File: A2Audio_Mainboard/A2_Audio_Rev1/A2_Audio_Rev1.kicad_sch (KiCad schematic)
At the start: 33 parts, among them J2 AudioJack3, J3 BOOT_JUMPER, SW1 SW_Push, SW2 WIFI_SLIDER, SW3 RotaryEncoder_Switch, SW4 BT_SLIDER, SW5 SW_PREV, SW6 SW_NEXT, SW7 SW_PLAY, U15 CM5108000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

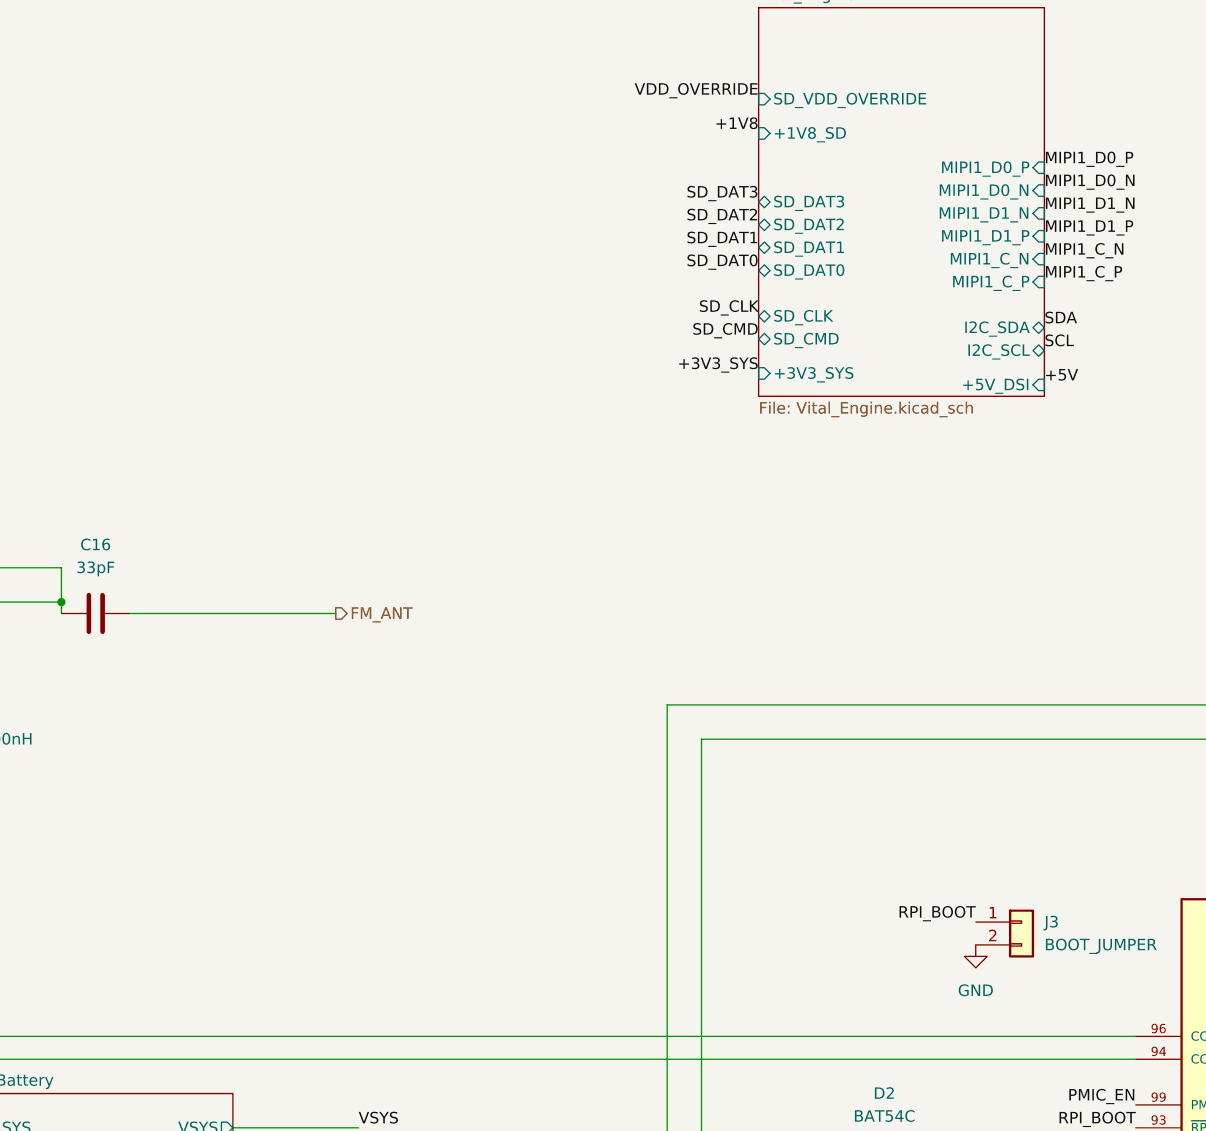
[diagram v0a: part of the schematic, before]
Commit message: Added footprints and a few more parts.
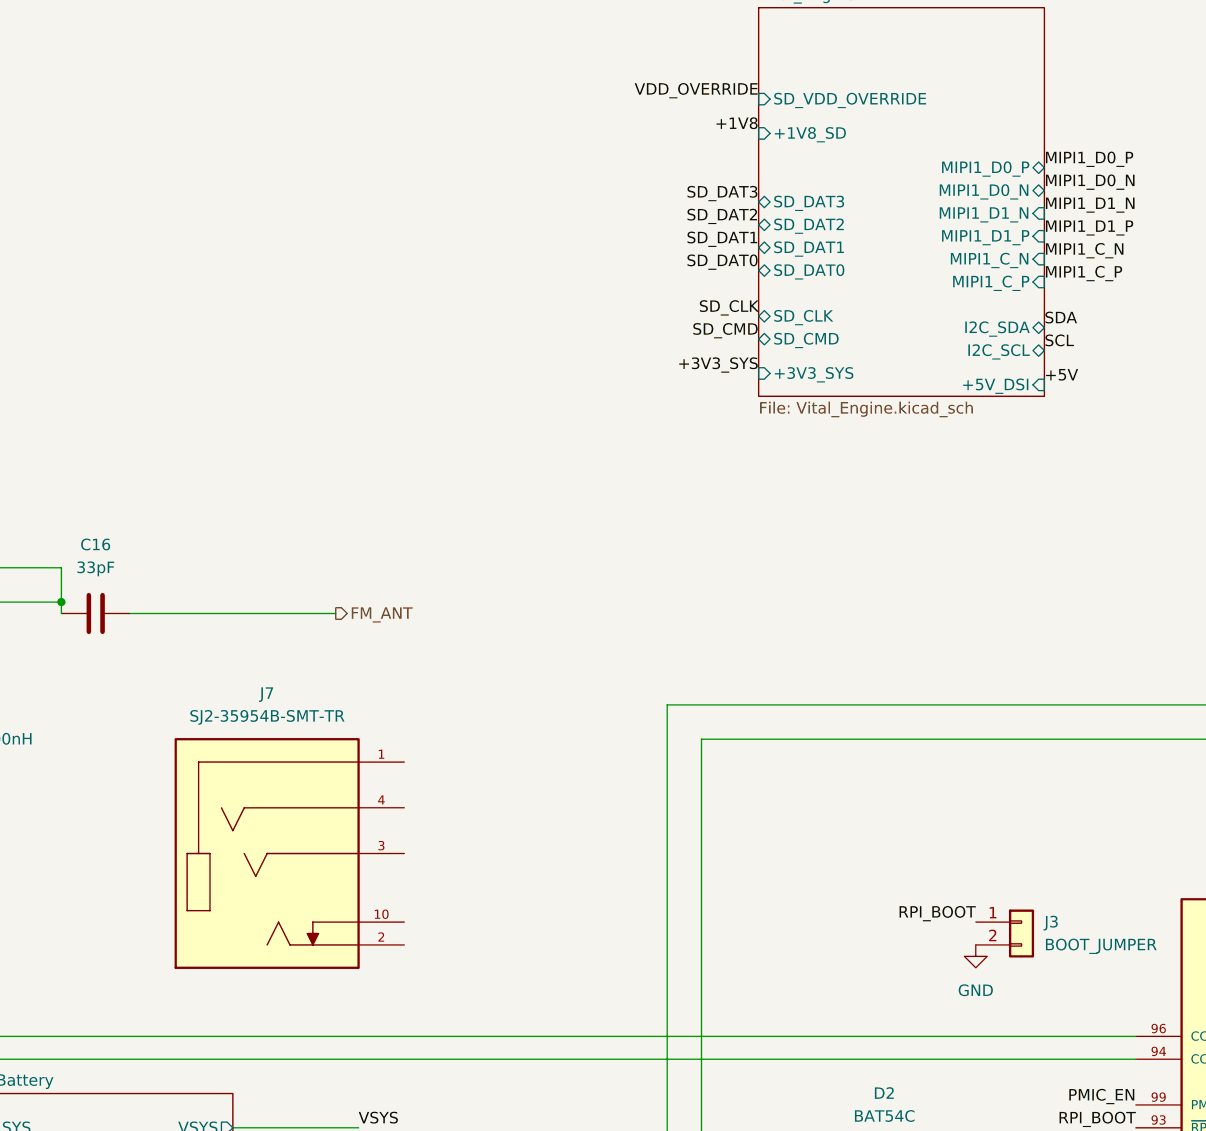
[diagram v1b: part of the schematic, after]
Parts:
- added J7: SJ2-35954B-SMT-TR, SJ2-35954B-SMT-TR:CUI_SJ2-35954B-SMT-TR, symbol SJ2-35954B-SMT-TR:SJ2-35954B-SMT-TR
- BT1: footprint (none) -> Battery:BatteryHolder_Keystone_3000_1x12mm
- C105, C106, C107, C108, C109, C110, C16, C82, C83: footprint (none) -> Capacitor_SMD:C_0402_1005Metric
- J3: footprint (none) -> TestPoint:TestPoint_2Pads_Pitch2.54mm_Drill0.8mm
- R29, R30, R41, R42, R43, R44, R45, R46, R47, R48: footprint (none) -> Resistor_SMD:R_0402_1005Metric

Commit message: More Refinement
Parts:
- removed C16: 33pF, Capacitor_SMD:C_0402_1005Metric, symbol symbols:C
- removed J2: AudioJack3, symbol symbols:AudioJack3
- removed L2: 100nH, symbol symbols:L
- added C103: 1µF, symbol symbols:C
- added C104: 100pF, symbol symbols:C
- added FB2: FerriteBead, symbol symbols:FerriteBead
- added R49: 2.2kΩ, symbol symbols:R
- added R50: 10kΩ, symbol symbols:R
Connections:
- net +3V3_SYS: now also R49.1
- net Audio_Engine/HP_OUT_L: now also J7.2
- net Audio_Engine/HP_OUT_R: now also J7.3
- net FM_ANT: now also C104.2
- net GND: now also FB2.2
- net at J7.1: now also C103.1, R49.2
- net at J7.4: now also C104.1, FB2.1
- new net: C103.2, R50.1
- new net MIC_IN: R50.2
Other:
- moved on the sheet: J7

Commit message: Refining of logic and adding battery connector
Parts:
- removed SW1: SW_Push, symbol symbols:SW_Push
- removed SW2: WIFI_SLIDER, symbol symbols:SW_SPDT
- removed SW4: BT_SLIDER, symbol symbols:SW_SPDT
- removed SW5: SW_PREV, symbol symbols:SW_Push
- removed SW6: SW_NEXT, symbol symbols:SW_Push
- removed SW7: SW_PLAY, symbol symbols:SW_Push
- added R54: 10kΩ, Resistor_SMD:R_0402_1005Metric, symbol symbols:R
- added SW1, SW4: SW_Wuerth_450301014042, Button_Switch_THT:SW_Slide-03_Wuerth-WS-SLTV_10x2.5x6.4_P2.54mm, symbol symbols:SW_Wuerth_450301014042
- added SW10, SW11, SW8, SW9: EVQ-PUJ02K, custom:SW_EVQPUJ_4P7X3P5_PAN, symbol 2026-05-23_05-33-27:EVQ-PUJ02K
- C103, C104: footprint (none) -> Capacitor_SMD:C_0402_1005Metric
- FB2: footprint (none) -> Inductor_SMD:L_0805_2012Metric
- J7: footprint SJ2-35954B-SMT-TR:CUI_SJ2-35954B-SMT-TR -> custom:CUI_SJ2-35954B-SMT-TR
- R49, R50: footprint (none) -> Resistor_SMD:R_0402_1005Metric
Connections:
- net +3V3_SYS: now also R54.2
- net BT: now also SW1.1 (B)
- net GND: now also SW1.2 (C), SW10.2, SW11.2, SW4.2 (C), SW8.2, SW9.2
- net NEXT: now also SW10.1
- net PLAY: now also SW11.1
- net PREV: now also SW9.1
- net WIFI: now also SW4.1 (B)
- net HP_DETECT: now reaches J7.10
- net HP_DETECT: now also U15.55 (GPIO14), R54.1
- net at D2.3: now also SW8.1
- net CARD_DETECT: now reaches U15.31 (GPIO12)
- net Power&Battery/CC1: no longer names the net of U15.94 (CC1)
- net Power&Battery/CC2: no longer names the net of U15.96 (CC2)
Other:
- sheet Power&Battery ports: added none; removed CC1, CC2
- sheet Recording&Radio_Engine ports: added MIC_IN; removed none
- sheet Vital_Engine ports: added CARD_DETECT; removed none

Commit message: Fixing ERC errors
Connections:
- net I2S_DATA_IN: now also U15.25 (GPIO21); no longer U15.27 (GPIO20)
- net I2S_DATA_OUT: now also U15.27 (GPIO20); no longer U15.25 (GPIO21)
